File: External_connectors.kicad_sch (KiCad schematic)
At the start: 16 parts, among them CN1 JST_Battery, J11 CAN_TX, J12 CAN_RX, J13 Conn_01x08, J14 Conn_01x06, J15 Conn_01x10, J16 Conn_01x08, J2 A - B, J21 U2U, J3 H - L, J4 TYPE-C-31-M12_13, J5 EXT_LOAD, J9 Conn_01x06

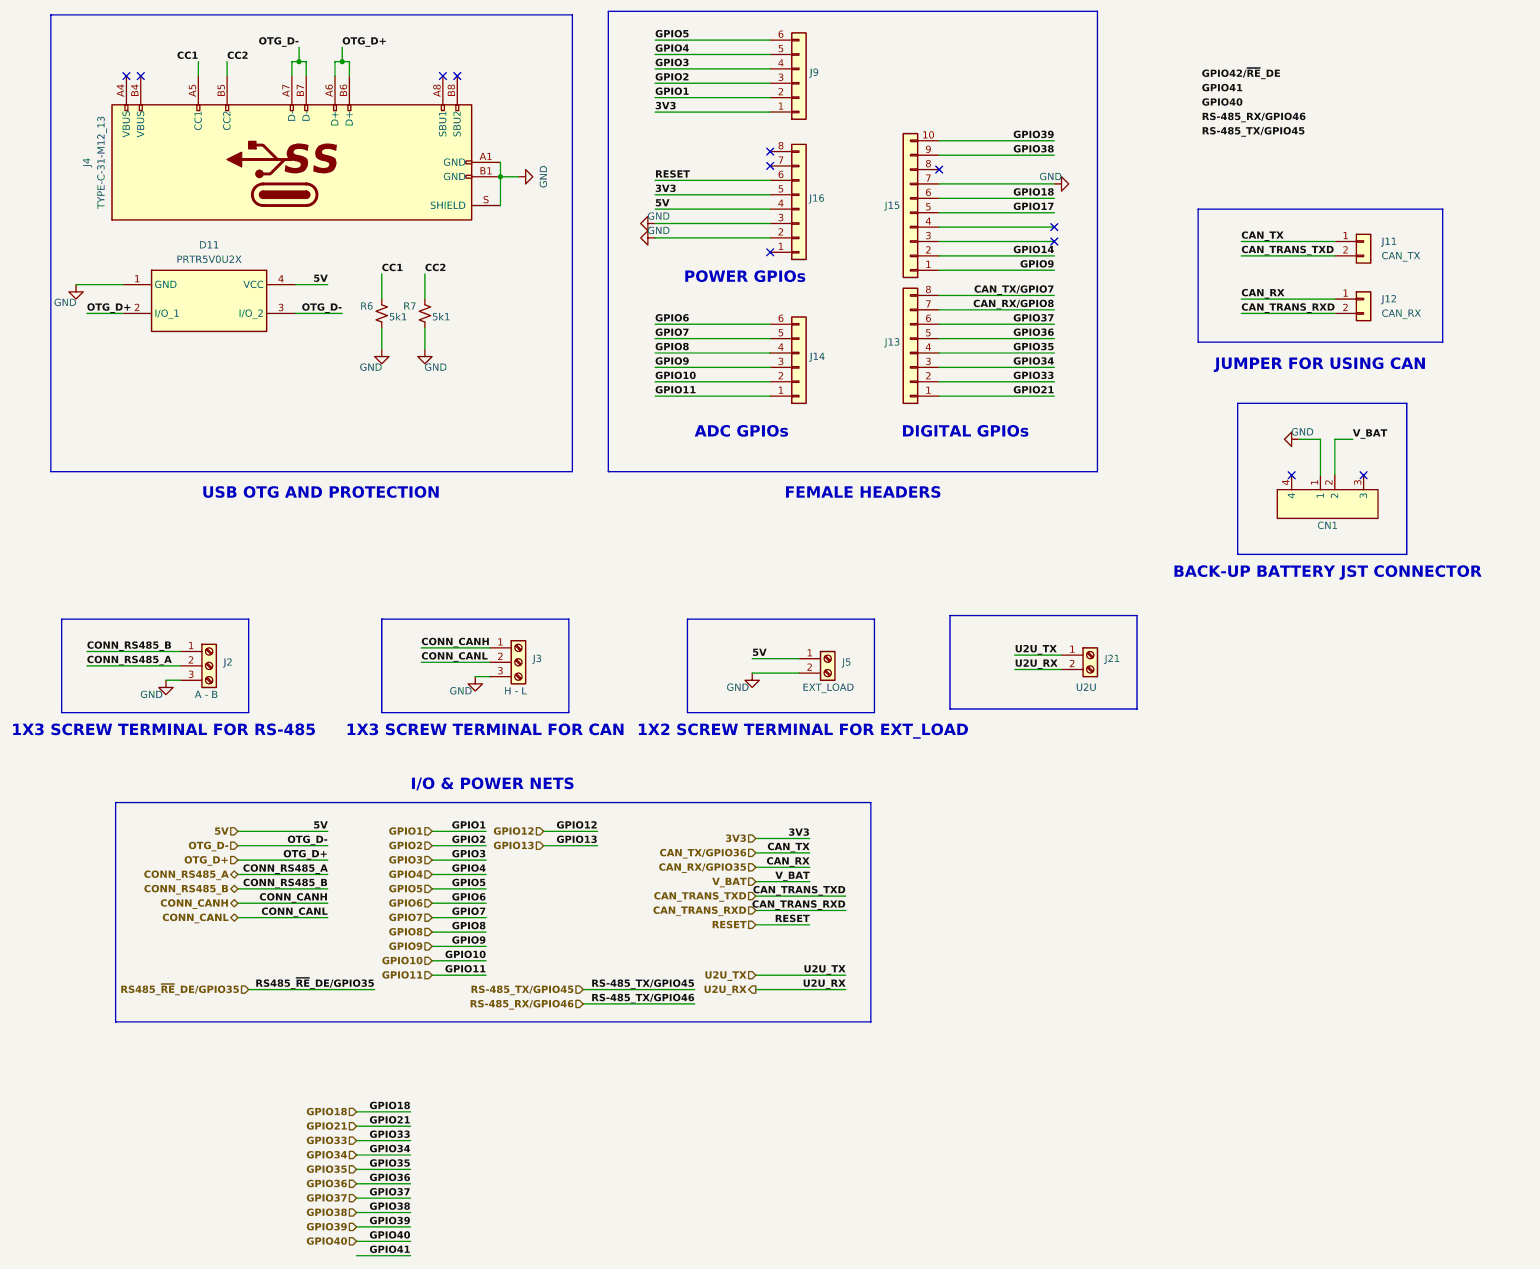
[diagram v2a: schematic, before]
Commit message: Completed routing for all GPIO pins
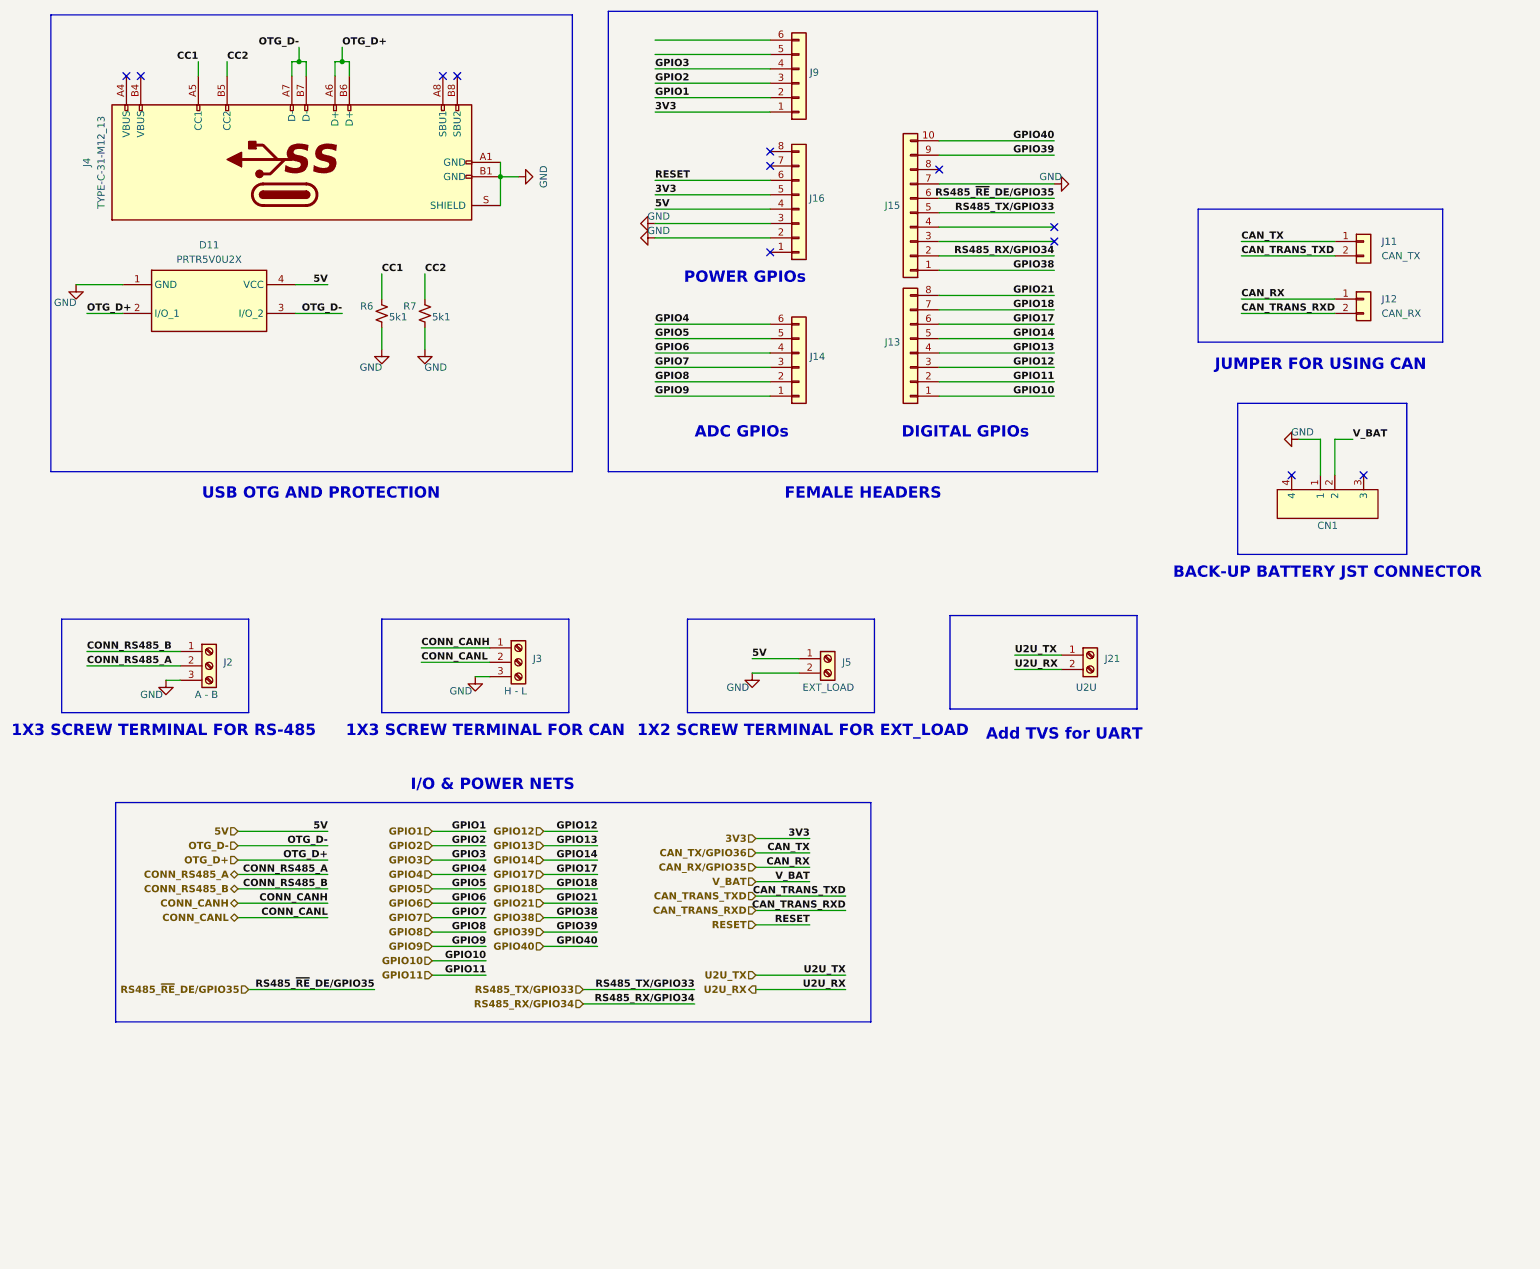
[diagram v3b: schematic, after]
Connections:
- net CAN_RX/GPIO8 is gone; now on net GPIO18: J13.7 (Pin_7)
- net CAN_TX/GPIO7 is gone; now on net GPIO21: J13.8 (Pin_8)
- net GPIO33 is gone; now on net GPIO11: J13.2 (Pin_2)
- net GPIO34 is gone; now on net GPIO12: J13.3 (Pin_3)
- net GPIO35 is gone; now on net GPIO13: J13.4 (Pin_4)
- net GPIO36 is gone; now on net GPIO14: J13.5 (Pin_5)
- net GPIO37 is gone; now on net GPIO17: J13.6 (Pin_6)
- net GPIO10: now also J13.1 (Pin_1); no longer J14.2 (Pin_2)
- net GPIO11: no longer J14.1 (Pin_1)
- net GPIO14: no longer J15.2 (Pin_2)
- net GPIO17: no longer J15.5 (Pin_5)
- net GPIO18: no longer J15.6 (Pin_6)
- net GPIO21: no longer J13.1 (Pin_1)
- net GPIO38: now also J15.1 (Pin_1); no longer J15.9 (Pin_9)
- net GPIO39: now also J15.9 (Pin_9); no longer J15.10 (Pin_10)
- net GPIO4: now also J14.6 (Pin_6); no longer J9.5 (Pin_5)
- net GPIO40: now also J15.10 (Pin_10)
- net GPIO5: now also J14.5 (Pin_5); no longer J9.6 (Pin_6)
- net GPIO6: now also J14.4 (Pin_4); no longer J14.6 (Pin_6)
- net GPIO7: now also J14.3 (Pin_3); no longer J14.5 (Pin_5)
- net GPIO8: now also J14.2 (Pin_2); no longer J14.4 (Pin_4)
- net GPIO9: now also J14.1 (Pin_1); no longer J14.3 (Pin_3), J15.1 (Pin_1)
- net RS485_~{RE}_DE/GPIO35: now also J15.6 (Pin_6)
- new net RS485_RX/GPIO34: J15.2 (Pin_2)
- new net RS485_TX/GPIO33: J15.5 (Pin_5)
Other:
- note added: "Add TVS for UART"

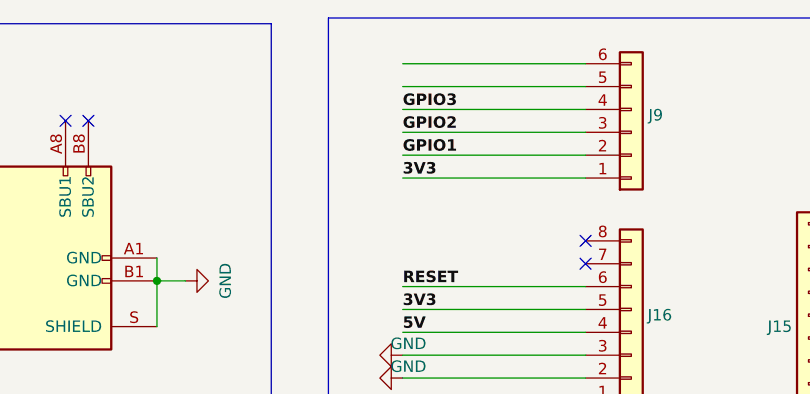
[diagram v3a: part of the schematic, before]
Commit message: Completed RS485 and CAN routing
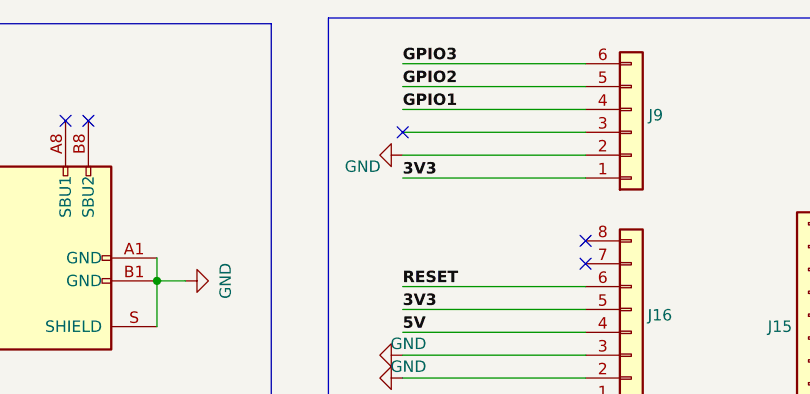
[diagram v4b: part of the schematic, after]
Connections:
- net GND: now also J9.2 (Pin_2)
- net GPIO1: now also J9.4 (Pin_4); no longer J9.2 (Pin_2)
- net GPIO2: now also J9.5 (Pin_5); no longer J9.3 (Pin_3)
- net GPIO3: now also J9.6 (Pin_6); no longer J9.4 (Pin_4)
- no-connect marks 12 -> 13
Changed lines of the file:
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@@
   (no_connect (at 92.075 27.94))
   (no_connect (at 33.655 27.94))
+  (no_connect (at 127 29.21))
   (no_connect (at 252.095 98.425))
   (no_connect (at 197.485 57.15))
@@
     (effects (font (size 1.27 1.27) bold (color 0 0 0 1)) (justify left bottom))
   )
-  (label "GPIO1" (at 127 31.75 0) (fields_autoplaced)
+  (label "GPIO1" (at 127 26.67 0) (fields_autoplaced)
     (effects (font (size 1.27 1.27) bold (color 72 0 0 1)) (justify left bottom))
   )
@@
     (effects (font (size 1.27 1.27) bold (color 72 0 0 1)) (justify right bottom))
   )
-  (label "GPIO3" (at 127 26.67 0) (fields_autoplaced)
+  (label "GPIO3" (at 127 21.59 0) (fields_autoplaced)
     (effects (font (size 1.27 1.27) bold (color 72 0 0 1)) (justify left bottom))
   )
@@
     (effects (font (size 1.27 1.27) bold (color 0 0 255 1)) (justify left bottom))
   )
-  (label "GPIO2" (at 127 29.21 0) (fields_autoplaced)
+  (label "GPIO2" (at 127 24.13 0) (fields_autoplaced)
     (effects (font (size 1.27 1.27) bold (color 72 0 0 1)) (justify left bottom))
   )
@@
         )
       )
+    )
+  )
+  (symbol (lib_id "ESP32-S3_DB:GND") (at 127 31.75 270) (unit 1)
+    (in_bom yes) (on_board yes) (dnp no)
+    (property "Reference" "#PWR066" (at 120.65 31.75 0)
+      (effects (font (size 1.27 1.27)) hide)
+    )
+    (property "Value" "GND" (at 122.555 33.02 90)
+      (effects (font (size 1.27 1.27)))
+    )
+    (property "Footprint" "" (at 127 31.75 0)
+      (effects (font (size 1.27 1.27)) hide)
+    )
+    (property "Datasheet" "" (at 127 31.75 0)
+      (effects (font (size 1.27 1.27)) hide)
+    )
+    (pin "1")
+    (instances
+      (project "ESP32-S3_DB"
+        (path "/b7fc4bd3-c219-4455-832b-8d795385dcf1/e2721808-ce0b-4b73-8382-0fd911e1c931"
+          (reference "#PWR066") (unit 1)
+        )
+      )

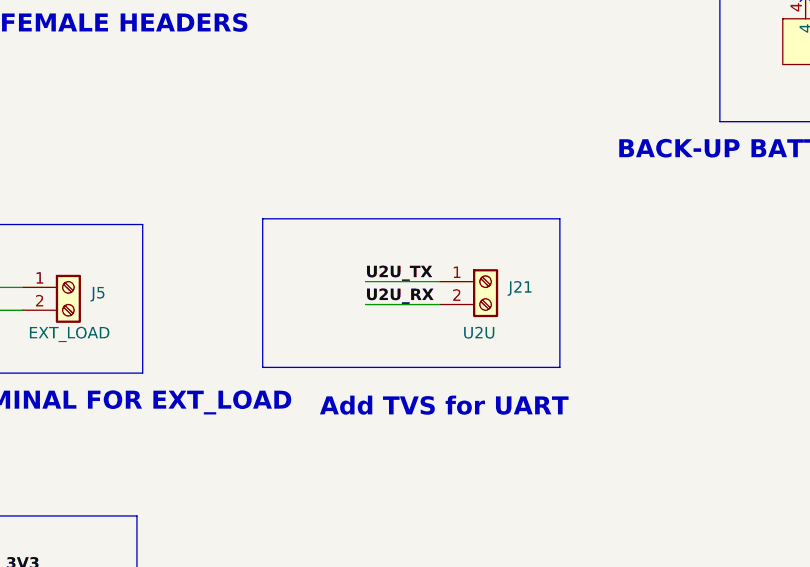
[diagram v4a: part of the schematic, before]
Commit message: Completed routing for USB peripheral for CH340
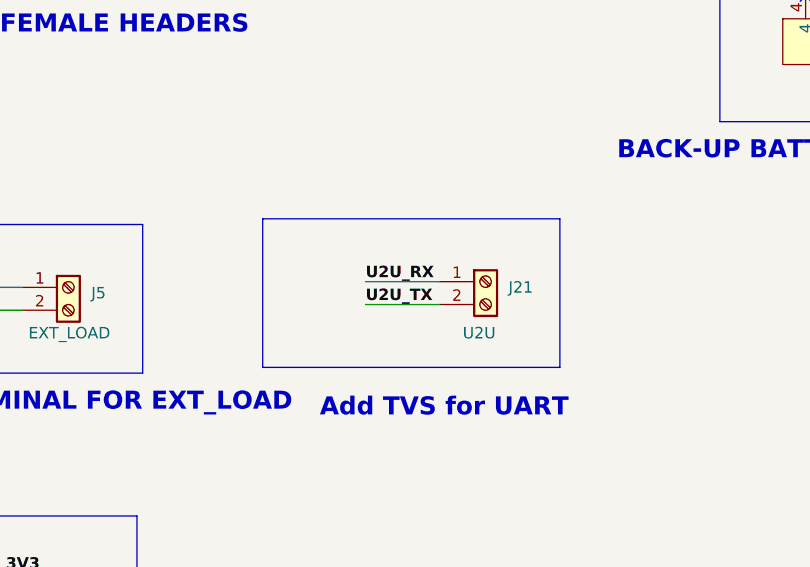
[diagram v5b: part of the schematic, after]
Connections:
- net U2U_RX: now also J21.1 (Pin_1); no longer J21.2 (Pin_2)
- net U2U_TX: now also J21.2 (Pin_2); no longer J21.1 (Pin_1)
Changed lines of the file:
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@@
     (effects (font (size 1.27 1.27) bold (color 0 0 0 1)) (justify left bottom))
   )
-  (label "U2U_TX" (at 190.5 130.175 0) (fields_autoplaced)
+  (label "U2U_TX" (at 190.5 132.715 0) (fields_autoplaced)
     (effects (font (size 1.27 1.27) bold (color 0 0 255 1)) (justify left bottom))
   )
@@
     (effects (font (size 1.27 1.27) bold (color 72 0 0 1)) (justify left bottom))
   )
-  (label "U2U_RX" (at 190.5 132.715 0) (fields_autoplaced)
+  (label "U2U_RX" (at 190.5 130.175 0) (fields_autoplaced)
     (effects (font (size 1.27 1.27) bold (color 0 0 255 1)) (justify left bottom))
   )
